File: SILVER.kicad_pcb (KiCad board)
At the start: 2 copper layers, 120 x 80 mm, 20 parts, among them J1 Conn_01x13, J10 Conn_02x22_Odd_Even_MountingP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, J11 UltraRight, J12 Conn_01x02_Pin, J14 Screw_Terminal_01x02, J15 Screw_Terminal_01x02, J16 Screw_Terminal_01x02, J17 Screw_Terminal_01x02, J18 Conn_01x02_Pin, J2 UltraLeft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

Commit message: PCB v3.0
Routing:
- net +3.3V: track 194.6 -> 255.0 mm
- net B1: track 115.8 -> 84.2 mm, vias 2 -> 0
- net B7: track 82.9 -> 114.4 mm, vias 2 -> 0
- net +5V: track 149.7 -> 175.4 mm, vias 0 -> 1
- net C5: track 71.0 -> 53.7 mm, vias 4 -> 0
- net B6: track 66.4 -> 79.4 mm, vias 1 -> 2
- net A4: track 47.2 -> 38.7 mm, vias 2 -> 0
- net A7: track 73.9 -> 66.6 mm, vias 3 -> 0
- net A6: track 50.6 -> 45.6 mm, vias 3 -> 0
- net A0: track 35.9 -> 31.5 mm, vias 4 -> 0
- net C1: track 36.1 -> 31.9 mm, vias 2 -> 0
- net E4: track 72.9 -> 76.5 mm
- net C4: track 54.5 -> 51.7 mm, vias 3 -> 0
- net NR: track 117.1 -> 115.0 mm
- net B0: track 56.0 -> 54.9 mm, vias 2 -> 0
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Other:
- outline, holes or cut-outs redrawn

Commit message: final
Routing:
- net B7: track 114.4 -> 88.4 mm, vias 0 -> 1
- net +5V: track 175.4 -> 190.9 mm
- net SWDIO: track 11.5 -> 3.69 mm
- net E4: track 76.5 -> 70.9 mm
- net +3.3V: track 255.0 -> 249.5 mm
- net OUTB_R: track 12.1 -> 10.0 mm
- net OUTA_R: track 10.9 -> 8.98 mm
- net NR: track 115.0 -> 113.3 mm
- net E6: track 25.8 -> 24.3 mm
- net B6: track 79.4 -> 80.6 mm
- net E8: track 86.1 -> 85.2 mm
- net B4: track 101.3 -> 100.6 mm
- net D13: track 89.7 -> 90.4 mm
- net E7: track 115.6 -> 114.9 mm
- net A7: track 66.6 -> 67.1 mm
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
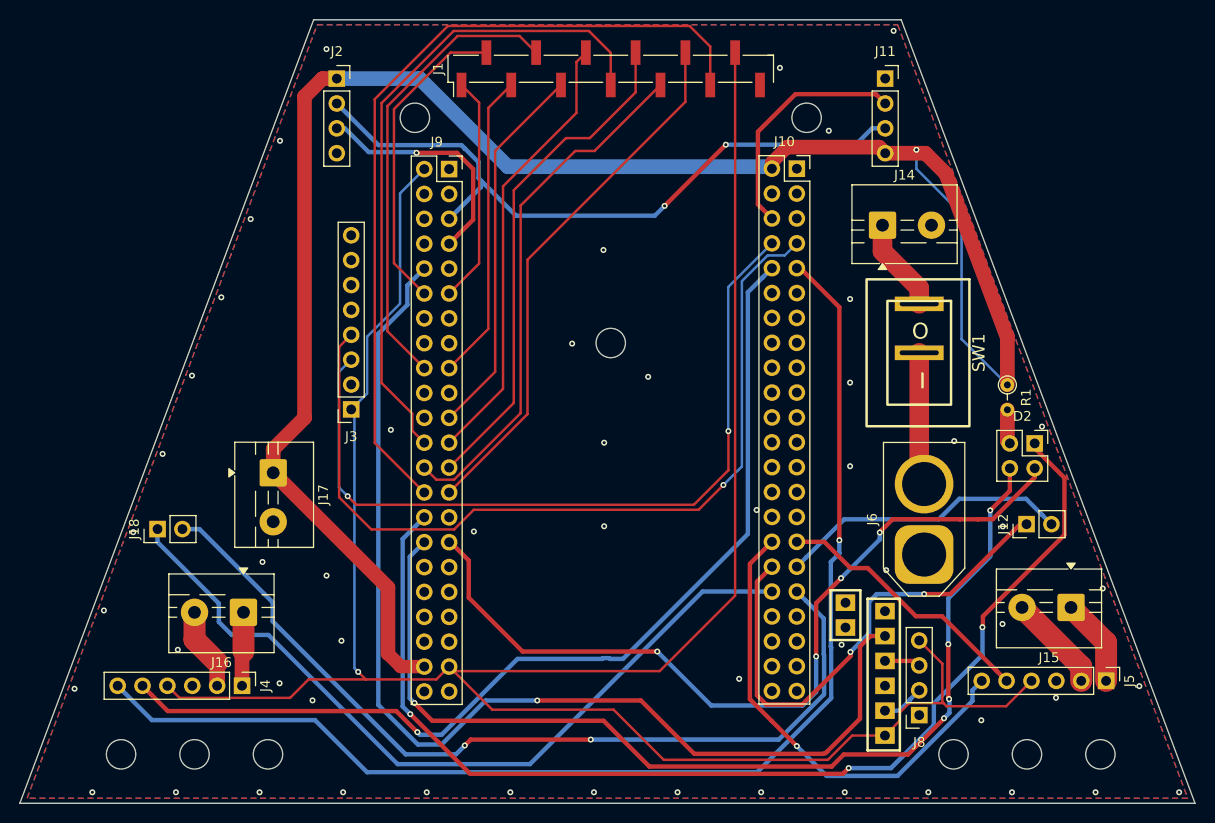
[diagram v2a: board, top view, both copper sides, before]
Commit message: feat: Update KiCad PCB design, regenerate manufacturing Gerber files, and refresh production outputs.
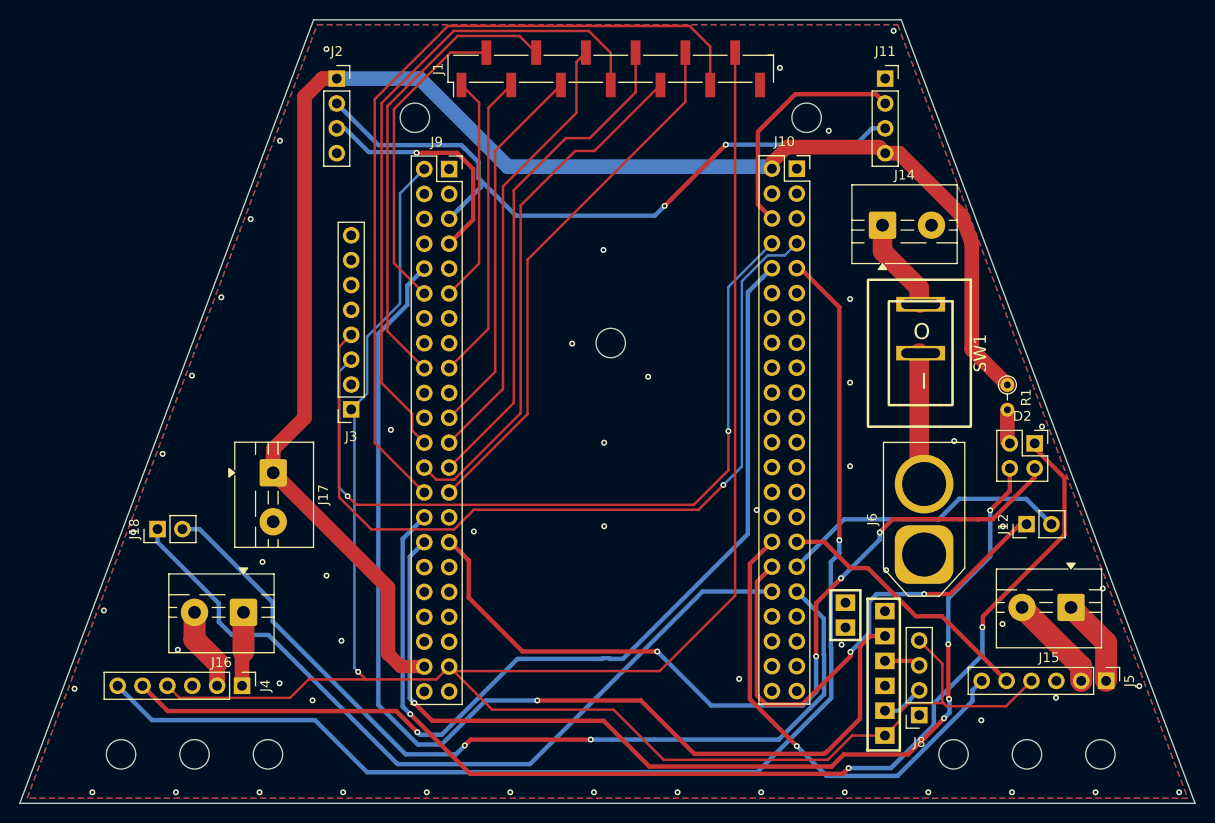
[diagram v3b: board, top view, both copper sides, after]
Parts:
- moved SW1 0.15 mm to (231.6, 104.0)
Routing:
- net +5V: track 190.9 -> 162.3 mm, vias 1 -> 0
